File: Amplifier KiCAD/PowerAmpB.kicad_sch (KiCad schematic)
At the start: 39 parts, among them Q11 BC546, Q12 BCM846BS-7, Q13 BC546, Q14 BC546, Q15 BD140, Q16 BC546, Q17 BD139, Q18 BD140, Q19 TIP36, Q20 TIP35

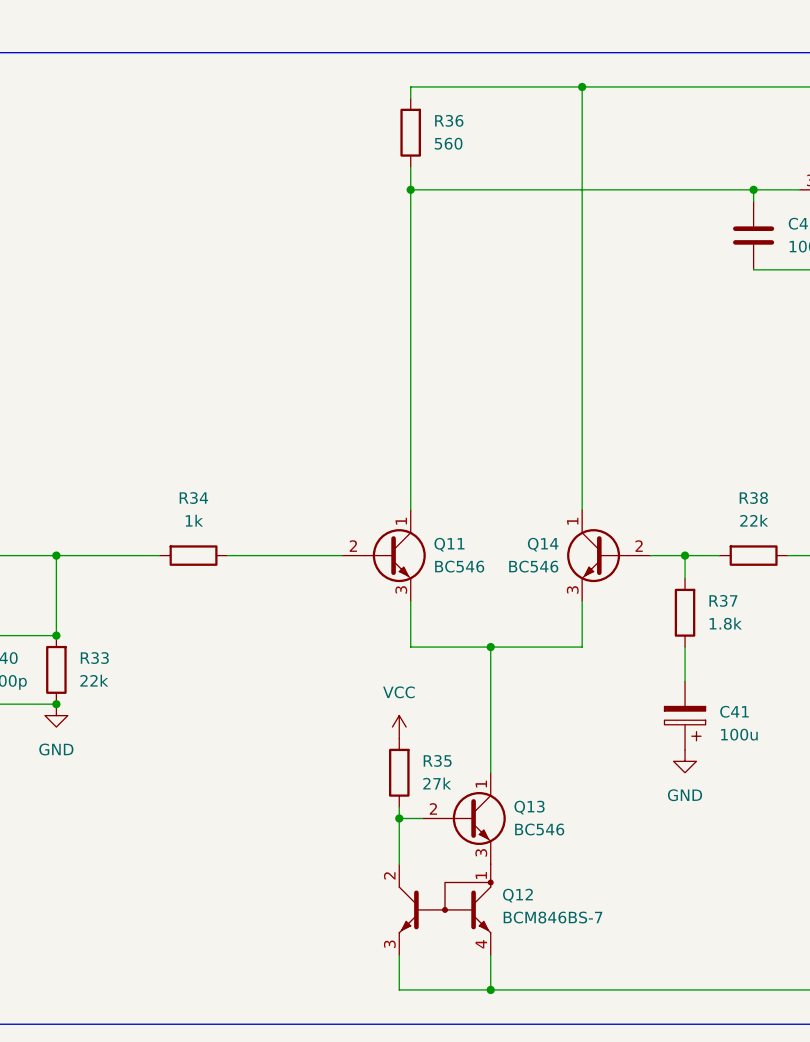
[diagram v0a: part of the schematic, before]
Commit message: Component Placement Finalised, Starting Traces
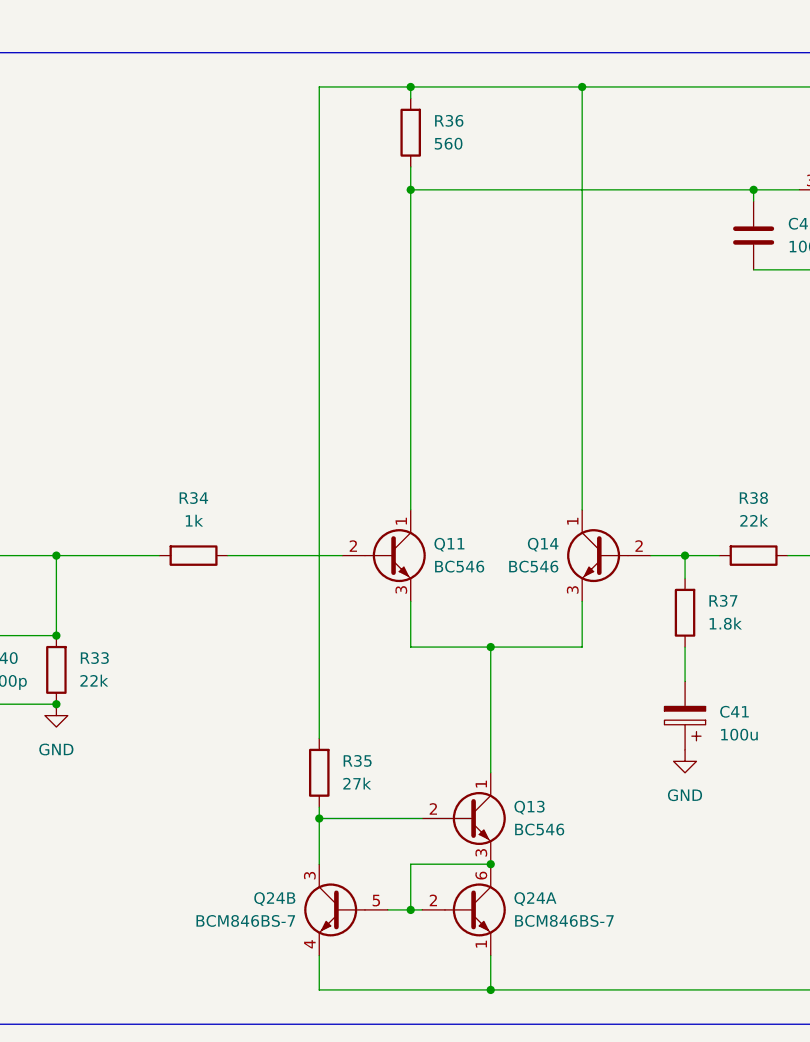
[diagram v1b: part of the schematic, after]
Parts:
- removed Q12: BCM846BS-7, Package_TO_SOT_SMD:SOT-363_SC-70-6, symbol Transistor_BJT:Q_Dual_NPN_C2C1E1E2
- added Q24: BCM846BS-7, Package_TO_SOT_SMD:SOT-363_SC-70-6, symbol Transistor_BJT:Q_Dual_NPN_NPN_C1E1C2E2B2B1
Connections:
- net VCC: no longer R35.2
- net at C45.2, C48.1, F4.1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: now also R35.2
- net at C47.1, C49.2, F3.1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: now also Q24.1 (E1), Q24.4 (E2)
- net at Q13.2 (B), R35.1: now also Q24.3 (C2)
- net at Q13.3 (E): now also Q24.2 (B1), Q24.5 (B2), Q24.6 (C1)
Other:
- moved on the sheet: R35
